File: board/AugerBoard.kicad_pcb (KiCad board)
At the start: 2 copper layers, 96.5 x 99.1 mm, 77 parts, among them J1 RJ45_LED_Shielded, J2 Conn_01x04_MountingPin, Q1 BSS138, Q2 BSS138, Q3 BSS138, Q4 BSS138, Q5 BSS138, Q6 BSS138, Q7 BSS138, Q8 BSS138, Q9 BSS138, SW1 SW_Push, SW10 SW_SPDT, SW2 SW_Push, SW3 SW_Push, SW4 SW_Push, SW5 SW_Push, SW6 SW_Push, SW7 SW_Push, SW8 SW_Push, SW9 SW_Push, U1 OKI 5V, U2 Teensy4.1_DEV-16771, U3 ATA6561, U4 OKI 3V3, U6 MAX3485

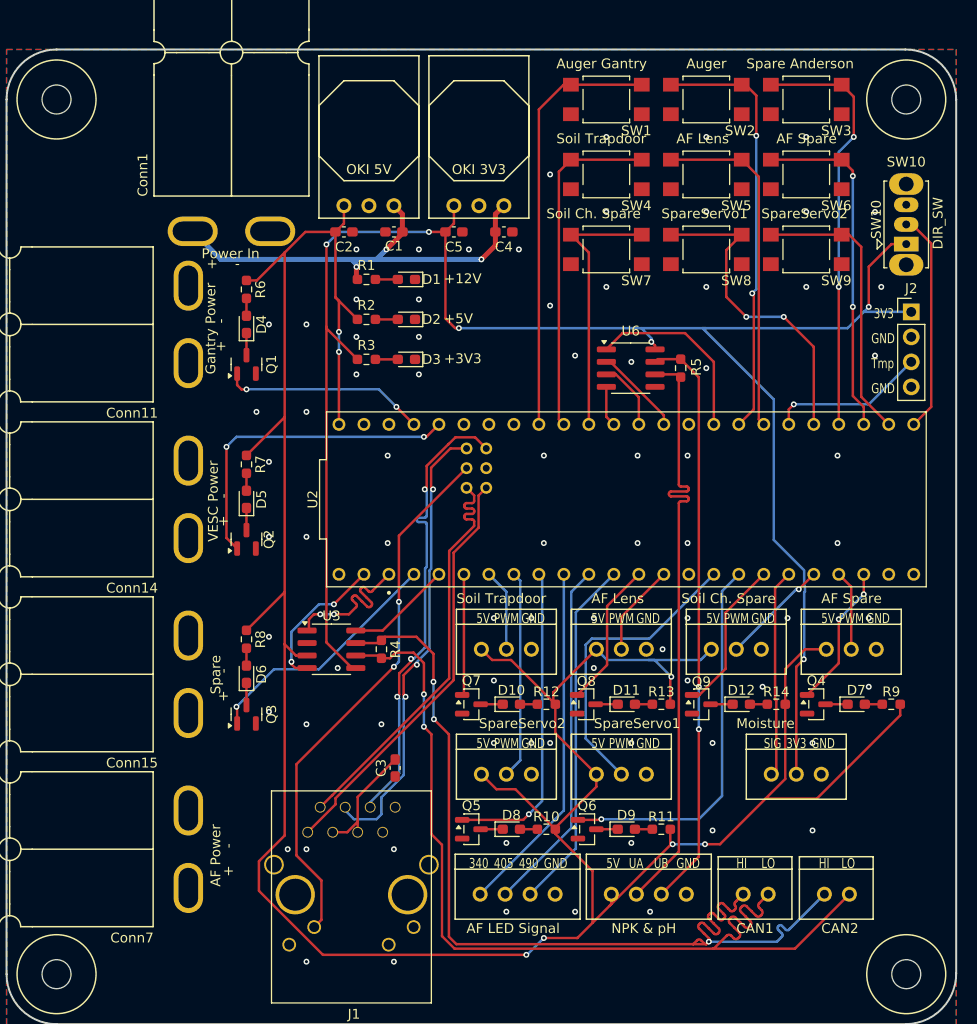
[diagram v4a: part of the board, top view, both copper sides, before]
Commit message: made minor design changes to layout
changed 12V plane dimensions, rerouted a few traces for clearance
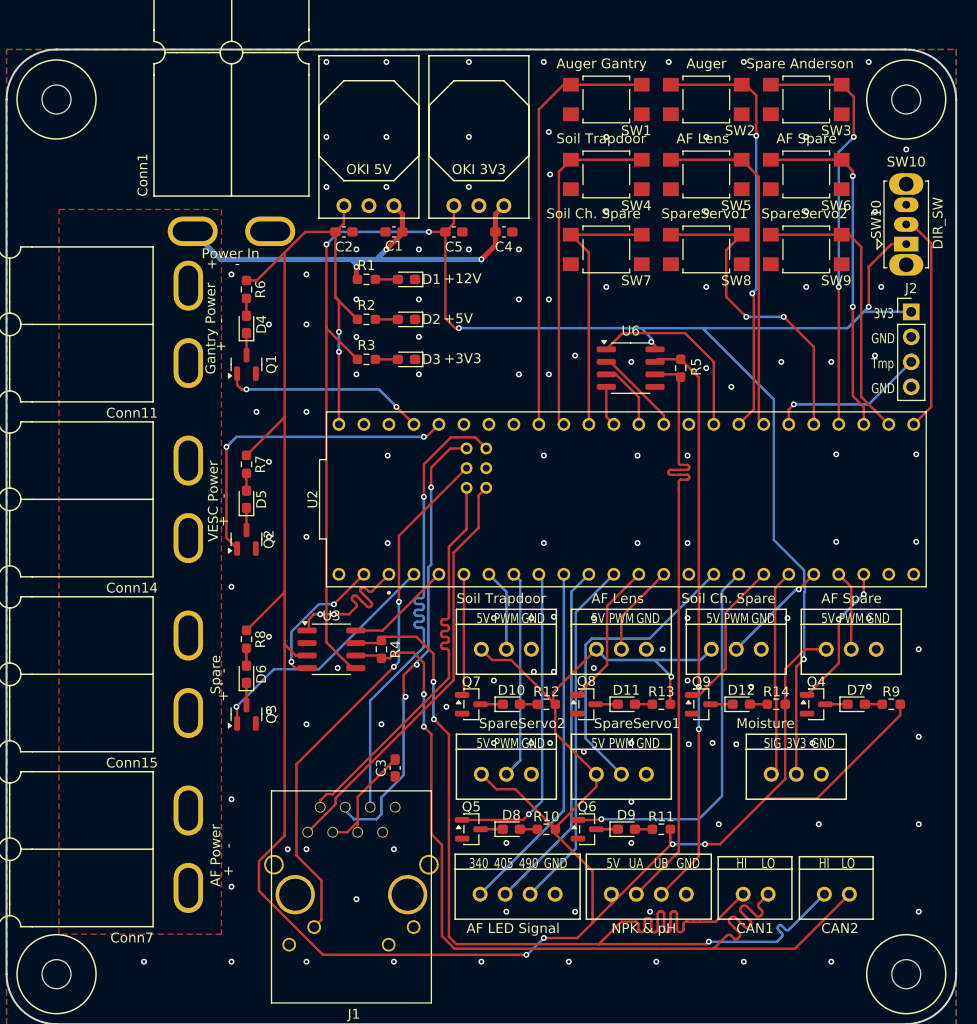
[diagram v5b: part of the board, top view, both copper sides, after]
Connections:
- U2 pad 3.3V_1: +3.3V -> unconnected-(U2-3.3V-Pad3.3V_1)_1
- U2 pad 3.3V_2: +3.3V -> unconnected-(U2-3.3V-Pad3.3V_1)
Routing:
- net Net-(U3-CANH): track 97.0 -> 108.2 mm
- net /Communications/R-: track 46.9 -> 49.3 mm, vias 3 -> 1
- net GND: vias 79 -> 127
- added copper zone on F.Cu, net +12V

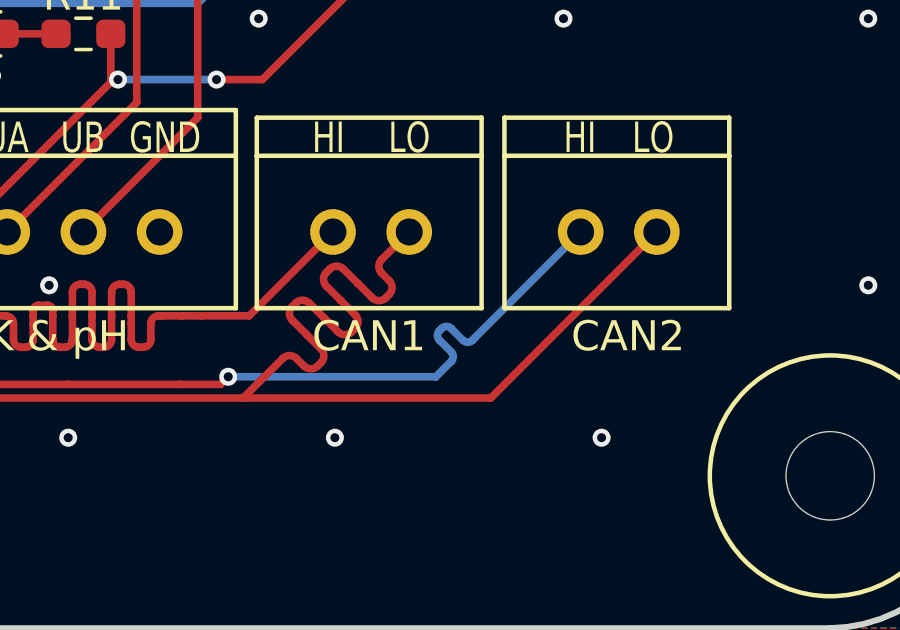
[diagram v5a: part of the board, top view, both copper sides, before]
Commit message: changed trace lengths
made minor changes to trace lengths of CAN lines
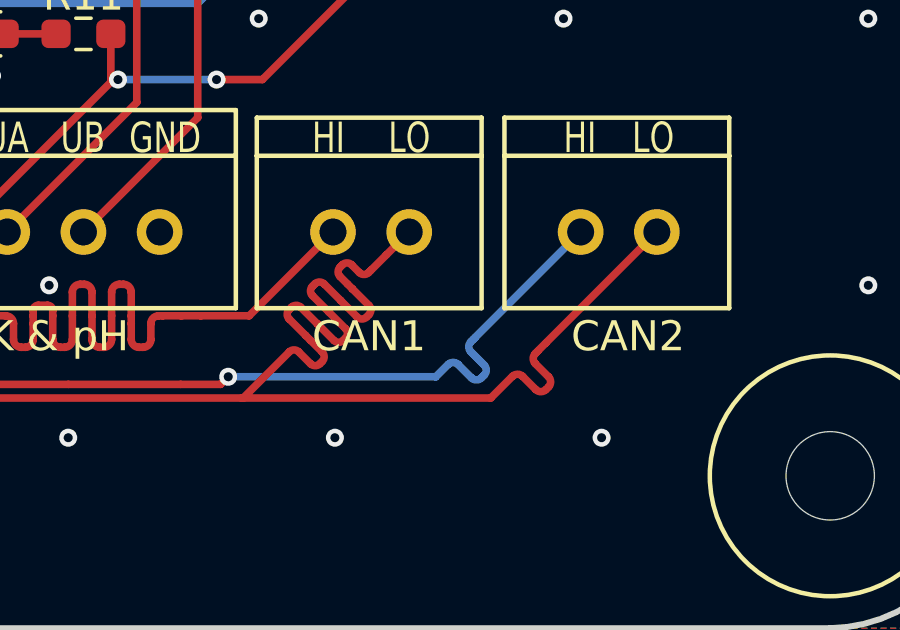
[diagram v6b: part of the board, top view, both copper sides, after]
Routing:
- net Net-(U3-CANL): track 95.9 -> 99.6 mm

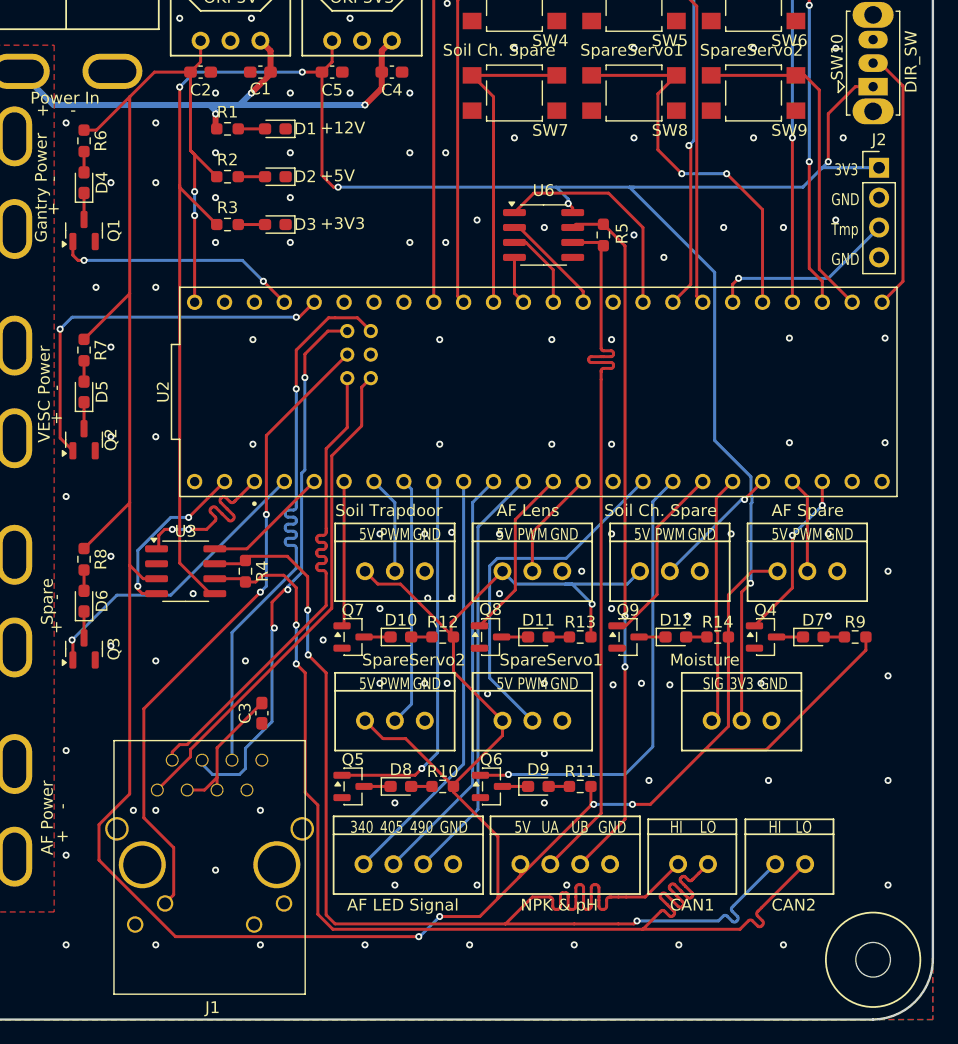
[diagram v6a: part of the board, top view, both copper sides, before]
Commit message: Added Second CAN and Switch
Retraced CAN signal lines and added a second transceiver going to a switch
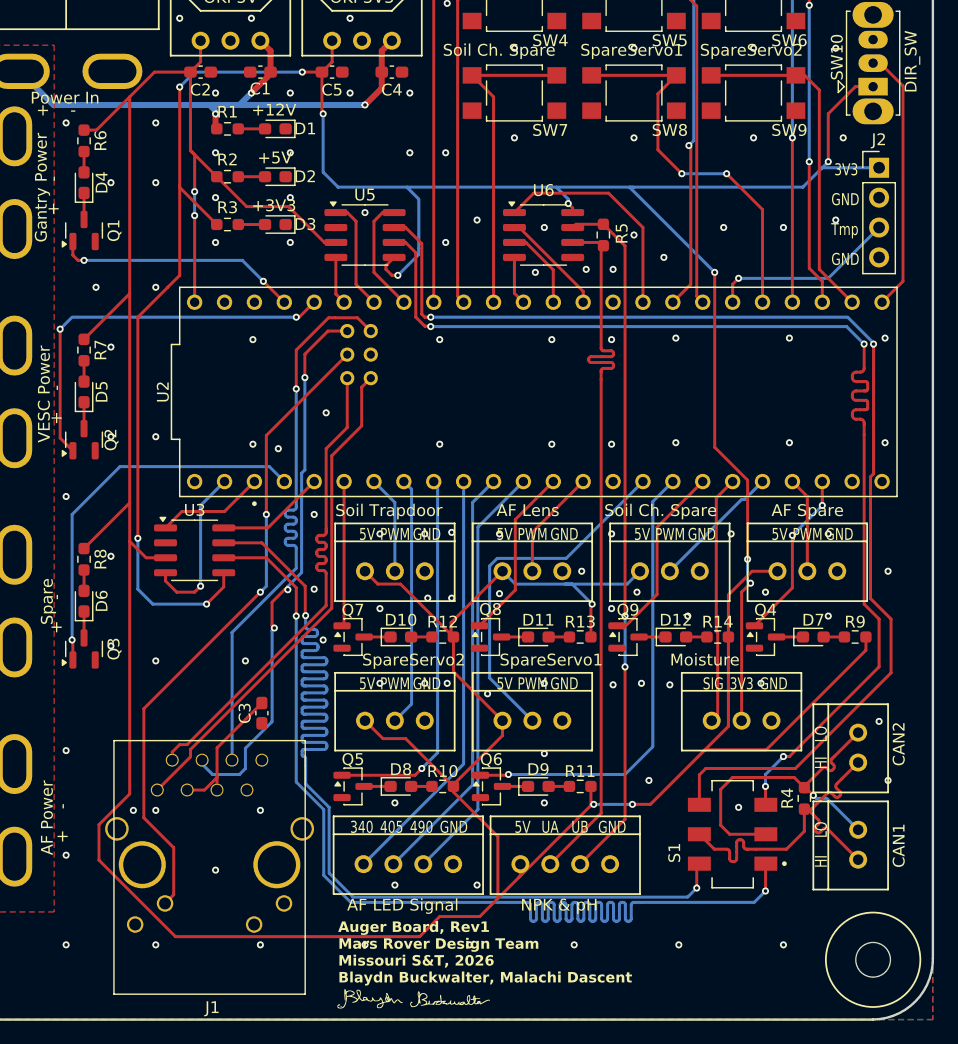
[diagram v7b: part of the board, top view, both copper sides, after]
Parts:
- added G***: LOGO, LOGO, F.Cu at (116.6, 156.0)
- added S1: SLW-913535-2A-SMT, MRDT_Switches:SW_SLW-913535-2A-SMT, F.Cu at (143.0, 141.7)
- added U5: ATA6561, Package_SO:SOIC-8_3.9x4.9mm_P1.27mm, F.Cu at (111.8, 90.8)
- moved R4 51.3 mm to (149.1, 138.7), turned to 90 degrees
- moved Conn12 15.3 mm to (153.7, 143.9), turned to 90 degrees
- moved Conn13 11.1 mm to (153.7, 135.6), turned to 90 degrees
- moved U3 1.93 mm to (97.3, 117.6)
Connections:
- net /Communications/RXD renamed /Communications/RXD1
- net /Communications/STBY renamed /Communications/STBY1
- net /Communications/TXD renamed /Communications/TXD1
- Conn12 pad 1: Net-(U3-CANH) -> Net-(Conn12-Pad1)
- Conn12 pad 2: Net-(U3-CANL) -> Net-(Conn12-Pad2)
- Conn13 pad 1: Net-(U3-CANH) -> Net-(Conn12-Pad1)
- Conn13 pad 2: Net-(U3-CANL) -> Net-(Conn12-Pad2)
- R4 pad 1: Net-(U3-CANH) -> Net-(Conn12-Pad1)
- R4 pad 2: Net-(U3-CANL) -> Net-(Conn12-Pad2)
- U2 pad 19: unconnected-(U2-A5-Pad19) -> /Communications/STBY2
- U2 pad 20: unconnected-(U2-A6-Pad20) -> /Communications/TXD2
- U2 pad 21: unconnected-(U2-A7-Pad21) -> /Communications/RXD2
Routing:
- net Net-(U5-CANH): track 0.00 -> 99.6 mm, vias 0 -> 2
- net Net-(U5-CANL): track 0.00 -> 96.4 mm, vias 0 -> 4
- net Net-(Conn12-Pad1): track 0.00 -> 30.1 mm
- net Net-(Conn12-Pad2): track 0.00 -> 28.7 mm, vias 0 -> 1
- net +3.3V: track 184.3 -> 204.7 mm, vias 6 -> 11
- net +5V: track 289.8 -> 303.1 mm, vias 7 -> 5
- net /Communications/STBY2: track 0.00 -> 9.95 mm
- net /Communications/TXD2: track 0.00 -> 9.53 mm
- net Net-(U3-CANH): track 108.4 -> 99.5 mm, vias 3 -> 2
- net /Power/SpareMotorLED: track 25.3 -> 32.6 mm
- net /Communications/TXD1: track 16.3 -> 9.19 mm, vias 2 -> 0
- net /Communications/RXD2: track 0.00 -> 4.10 mm
- net /Communications/STBY1: track 10.8 -> 9.32 mm
- net /Communications/RXD1: track 14.8 -> 14.0 mm, vias 2 -> 1
- net GND: vias 127 -> 135
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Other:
- board text added: "Auger Board, Rev1 Mars Rover Design Team Missouri S&T, 2026 Blaydn Buckwalter, Malachi Dascent"

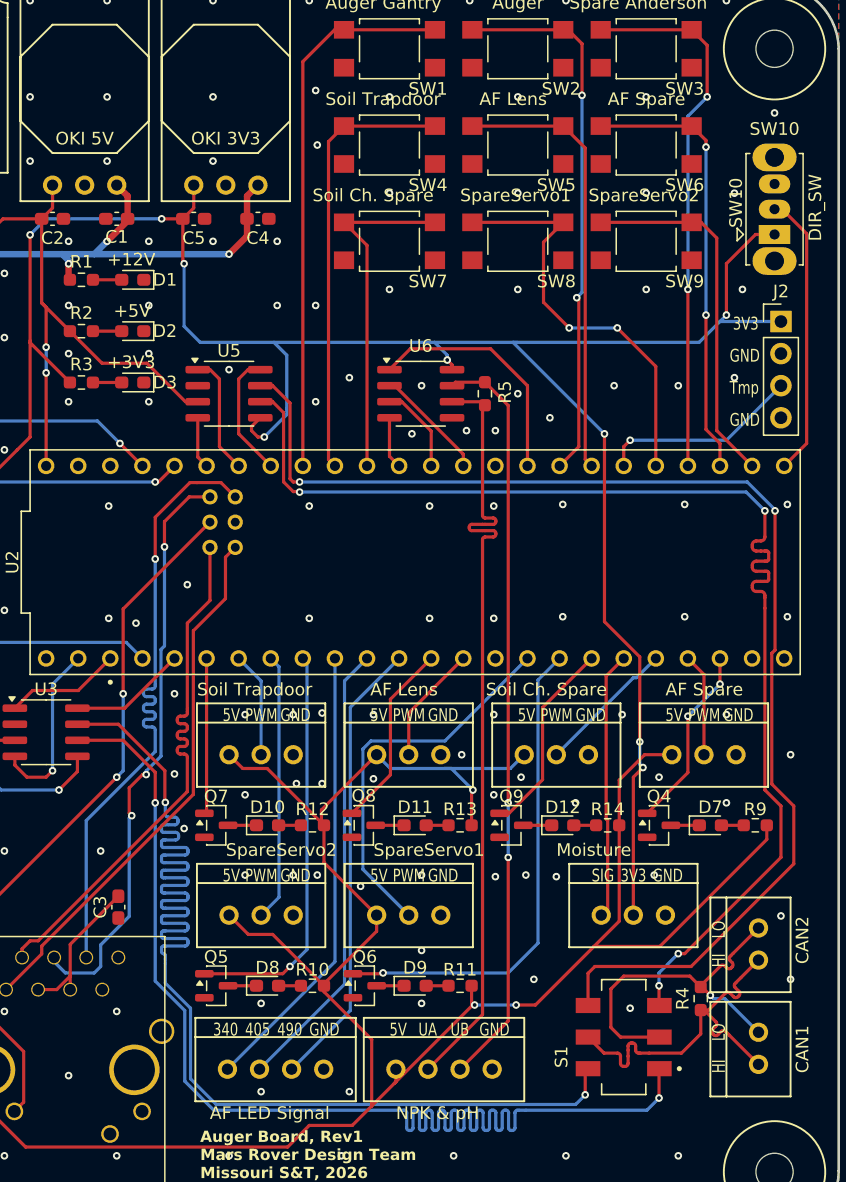
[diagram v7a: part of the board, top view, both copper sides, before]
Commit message: Equalized traces, text resizing
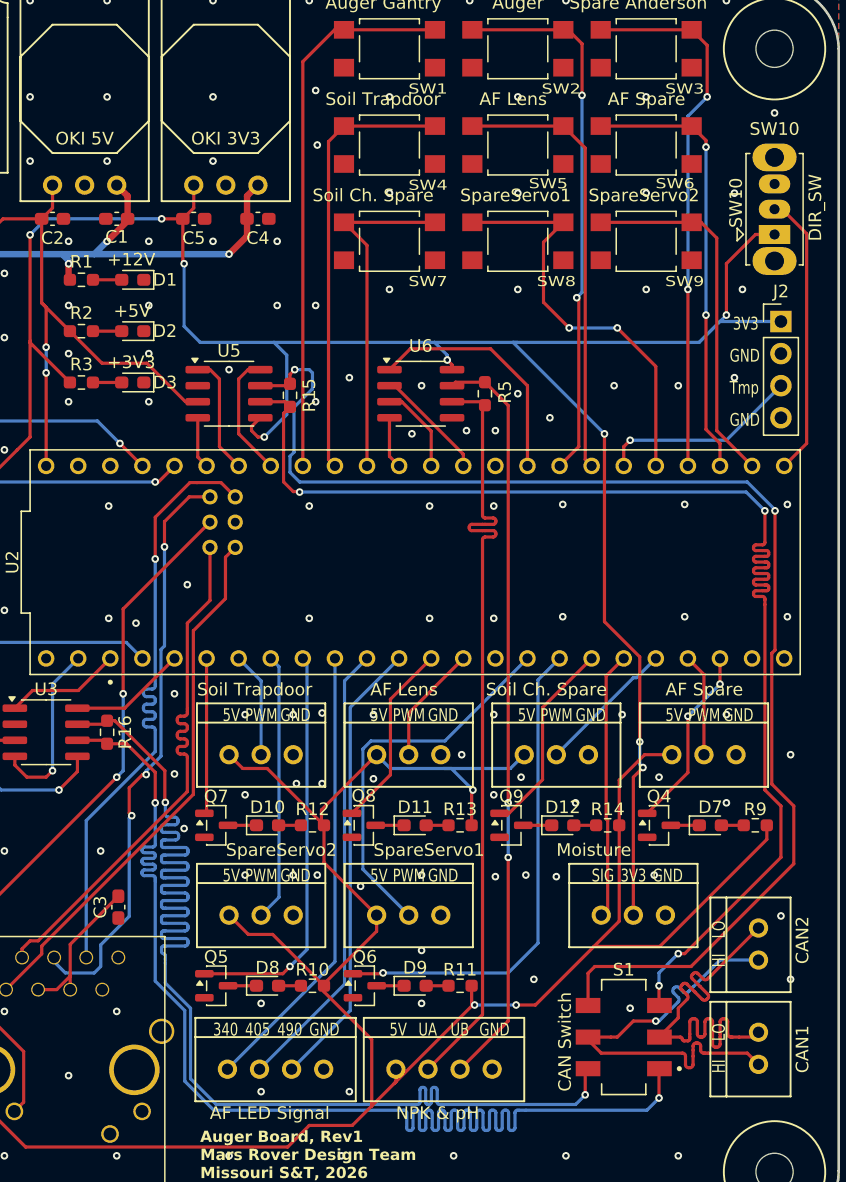
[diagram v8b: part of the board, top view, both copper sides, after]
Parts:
- removed R4: 120, Resistor_SMD:R_0603_1608Metric_Pad0.98x0.95mm_HandSolder
- added R15: 120, Resistor_SMD:R_0603_1608Metric_Pad0.98x0.95mm_HandSolder, F.Cu at (116.6, 90.9)
- added R16: 120, Resistor_SMD:R_0603_1608Metric_Pad0.98x0.95mm_HandSolder, F.Cu at (102.1, 117.6)
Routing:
- net Net-(Conn12-Pad2): track 28.7 -> 35.1 mm, vias 1 -> 0
- net Net-(U3-CANL): track 99.2 -> 104.5 mm
- net Net-(U5-CANH): track 99.6 -> 104.7 mm
- net Net-(U5-CANL): track 96.4 -> 101.5 mm
- net Net-(U3-CANH): track 99.5 -> 104.4 mm
- net Net-(Conn12-Pad1): track 30.1 -> 35.1 mm, vias 0 -> 1
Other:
- board text added: "CAN Switch"
